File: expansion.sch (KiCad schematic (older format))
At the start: 4 parts, among them J10 Conn_02x05_Odd_Even, J7 DF40HC(3.5)-60DS, J9 DF40HC(3.5)-60DS, U1 IMX8MM

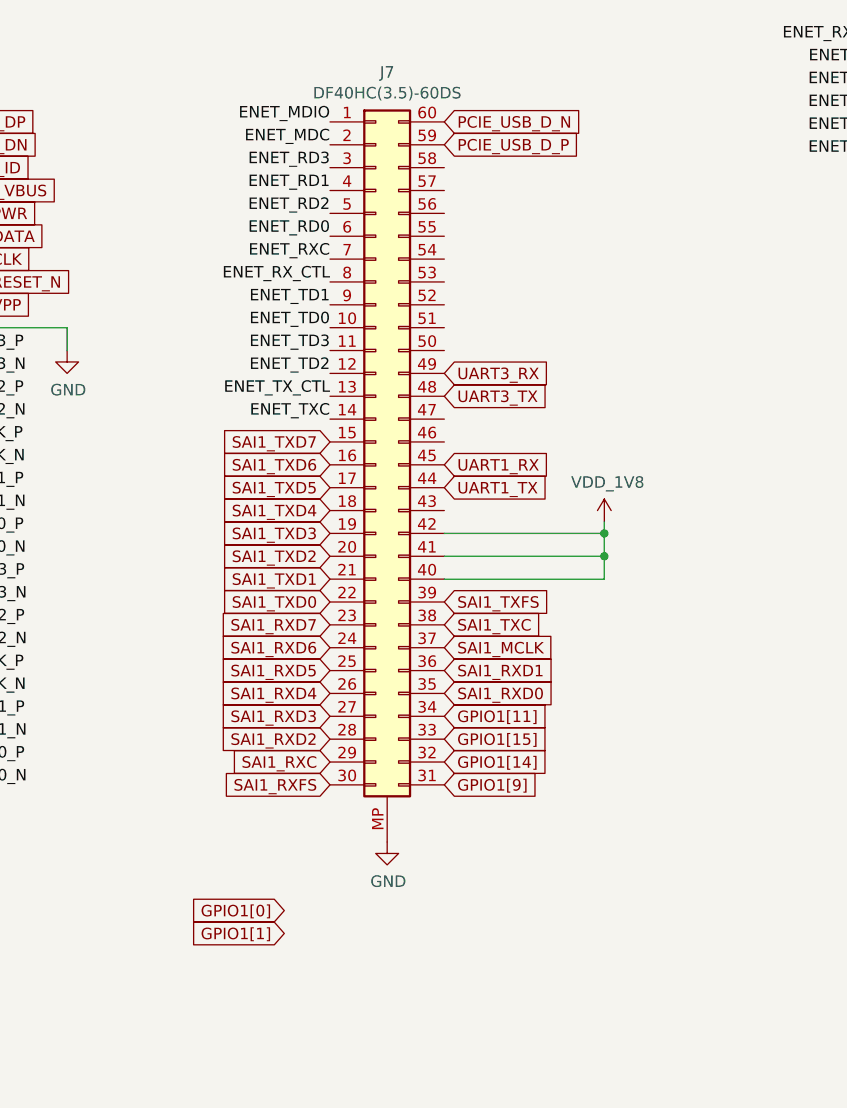
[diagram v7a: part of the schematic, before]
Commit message: prior to rerouting sai lanes
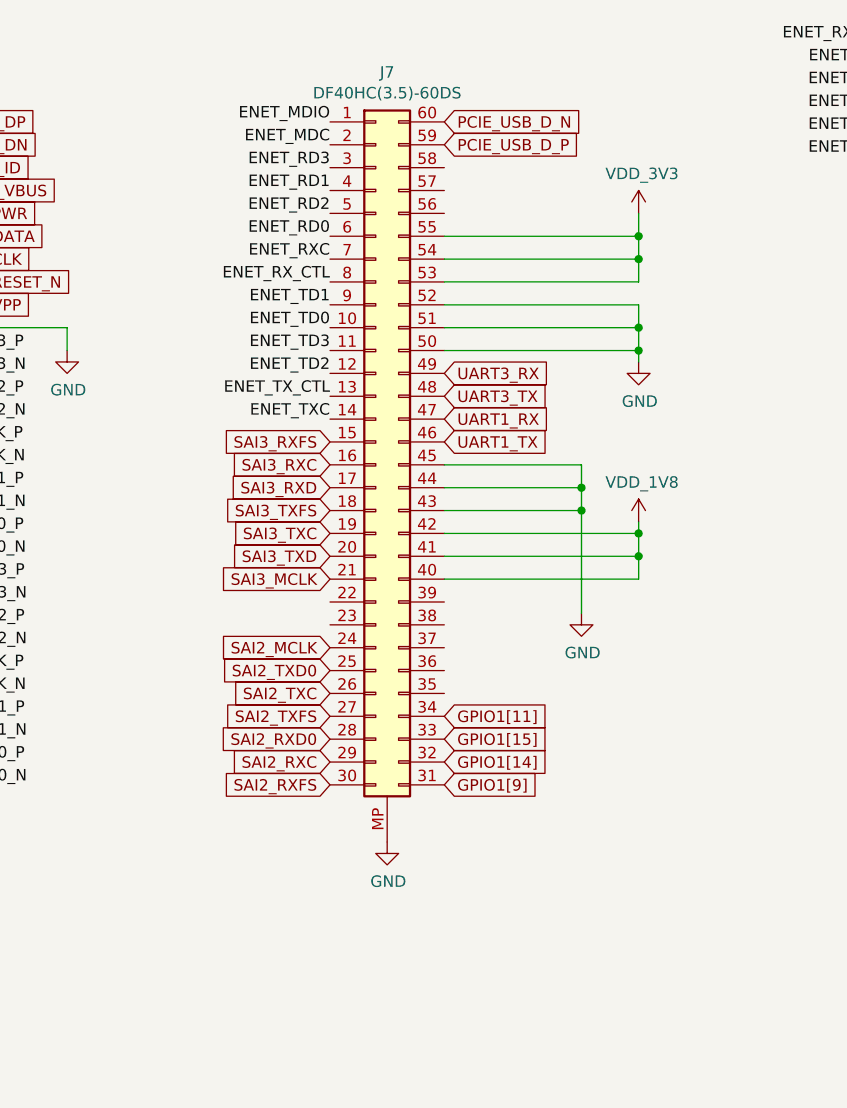
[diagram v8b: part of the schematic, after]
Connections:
- net GND: now also J7.43 (Pin_43), J7.44 (Pin_44), J7.45 (Pin_45), J7.50 (Pin_50), J7.51 (Pin_51), J7.52 (Pin_52)
- net UART1_RX: now also J7.47 (Pin_47); no longer J7.45 (Pin_45)
- net UART1_TX: now also J7.46 (Pin_46); no longer J7.44 (Pin_44)
- net VDD_3V3: now reaches J7.53 (Pin_53)
- net VDD_3V3: now also J7.54 (Pin_54), J7.55 (Pin_55)
- net SAI1_MCLK: no longer names the net of J7.37 (Pin_37)
- net SAI1_RXC renamed SAI2_RXC
- net SAI1_RXD0: no longer names the net of J7.35 (Pin_35)
- net SAI1_RXD1: no longer names the net of J7.36 (Pin_36)
- net SAI1_RXD2 renamed SAI2_RXD0
- net SAI1_RXD3 renamed SAI2_TXFS
- net SAI1_RXD4 renamed SAI2_TXC
- net SAI1_RXD5 renamed SAI2_TXD0
- net SAI1_RXD6 renamed SAI2_MCLK
- net SAI1_RXD7: no longer names the net of J7.23 (Pin_23)
- net SAI1_RXFS renamed SAI2_RXFS
- net SAI1_TXC: no longer names the net of J7.38 (Pin_38)
- net SAI1_TXD0: no longer names the net of J7.22 (Pin_22)
- net SAI1_TXD1 renamed SAI3_MCLK
- net SAI1_TXD2 renamed SAI3_TXD
- net SAI1_TXD3 renamed SAI3_TXC
- net SAI1_TXD4 renamed SAI3_TXFS
- net SAI1_TXD5 renamed SAI3_RXD
- net SAI1_TXD6 renamed SAI3_RXC
- net SAI1_TXD7 renamed SAI3_RXFS
- net SAI1_TXFS: no longer names the net of J7.39 (Pin_39)
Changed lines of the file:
@@
 Text Label 2750 2700 0    50   ~ 0
 GPIO3[17]
-Text GLabel 6550 6000 0    50   Input ~ 0
-GPIO1[0]
-Text GLabel 6550 6100 0    50   Input ~ 0
-GPIO1[1]
 $Comp
 L mxenc:MIMX8MM6DVTLZAA U1
@@
 Text Label 6750 2750 2    50   ~ 0
 ENET_RD3
-Text GLabel 6750 3950 0    50   Input ~ 0
-SAI1_TXD7
-Text GLabel 6750 4050 0    50   Input ~ 0
-SAI1_TXD6
-Text GLabel 6750 4150 0    50   Input ~ 0
-SAI1_TXD5
-Text GLabel 6750 4250 0    50   Input ~ 0
-SAI1_TXD4
-Text GLabel 6750 4350 0    50   Input ~ 0
-SAI1_TXD3
-Text GLabel 6750 4450 0    50   Input ~ 0
-SAI1_TXD2
-Text GLabel 6750 4550 0    50   Input ~ 0
-SAI1_TXD1
-Text GLabel 6750 4650 0    50   Input ~ 0
-SAI1_TXD0
-Text GLabel 6750 4750 0    50   Input ~ 0
-SAI1_RXD7
-Text GLabel 6750 4850 0    50   Input ~ 0
-SAI1_RXD6
-Text GLabel 6750 4950 0    50   Input ~ 0
-SAI1_RXD5
-Text GLabel 6750 5050 0    50   Input ~ 0
-SAI1_RXD4
-Text GLabel 6750 5150 0    50   Input ~ 0
-SAI1_RXD3
-Text GLabel 6750 5250 0    50   Input ~ 0
-SAI1_RXD2
-Text GLabel 6750 5350 0    50   Input ~ 0
-SAI1_RXC
-Text GLabel 6750 5450 0    50   Input ~ 0
-SAI1_RXFS
-Text GLabel 7250 4950 2    50   Input ~ 0
-SAI1_RXD1
-Text GLabel 7250 5050 2    50   Input ~ 0
-SAI1_RXD0
-Text GLabel 7250 4750 2    50   Input ~ 0
-SAI1_TXC
-Text GLabel 7250 4650 2    50   Input ~ 0
-SAI1_TXFS
-Text GLabel 7250 4850 2    50   Input ~ 0
-SAI1_MCLK
 Text Label 2750 2800 0    50   ~ 0
 GPIO3[18]
@@
 L mxenc:VDD_1V8 #PWR0223
 U 1 1 5F46F757
-P 7950 4300
-F 0 "#PWR0223" H 7950 4150 50  0001 C CNN
-F 1 "VDD_1V8" H 7965 4473 50  0000 C CNN
-F 2 "" H 7950 4300 50  0001 C CNN
-F 3 "" H 7950 4300 50  0001 C CNN
-	1    7950 4300
-	1    0    0    -1
-$EndComp
-Wire Wire Line
-	7950 4300 7950 4350
-Wire Wire Line
-	7950 4550 7250 4550
-Wire Wire Line
-	7250 4450 7950 4450
-Connection ~ 7950 4450
-Wire Wire Line
-	7950 4450 7950 4550
-Wire Wire Line
-	7950 4350 7250 4350
-Connection ~ 7950 4350
-Wire Wire Line
-	7950 4350 7950 4450
+P 8100 4300
+F 0 "#PWR0223" H 8100 4150 50  0001 C CNN
+F 1 "VDD_1V8" H 8115 4473 50  0000 C CNN
+F 2 "" H 8100 4300 50  0001 C CNN
+F 3 "" H 8100 4300 50  0001 C CNN
+	1    8100 4300
+	1    0    0    -1
+$EndComp
+Wire Wire Line
+	8100 4300 8100 4350
+Wire Wire Line
+	8100 4550 7250 4550
+Wire Wire Line
+	7250 4450 8100 4450
+Connection ~ 8100 4450
+Wire Wire Line
+	8100 4450 8100 4550
+Wire Wire Line
+	8100 4350 7250 4350
+Connection ~ 8100 4350
+Wire Wire Line
+	8100 4350 8100 4450
 Text GLabel 7250 2550 2    50   Input ~ 0
 PCIE_USB_D_N
@@
 Text GLabel 7250 3650 2    50   Input ~ 0
 UART3_RX
-Text GLabel 7250 4050 2    50   Input ~ 0
+Text GLabel 7250 3850 2    50   Input ~ 0
 UART1_RX
-Text GLabel 7250 4150 2    50   Input ~ 0
+Text GLabel 7250 3950 2    50   Input ~ 0
 UART1_TX
 $Comp
@@
 Text GLabel 7250 5250 2    50   Input ~ 0
 GPIO1[15]
+$Comp
+L power:GND #PWR0222
+U 1 1 5EFF4815
+P 7850 4700
+F 0 "#PWR0222" H 7850 4450 50  0001 C CNN
+F 1 "GND" H 7855 4527 50  0000 C CNN
+F 2 "" H 7850 4700 50  0001 C CNN
+F 3 "" H 7850 4700 50  0001 C CNN
+	1    7850 4700
+	1    0    0    -1
+$EndComp
+Wire Wire Line
+	7250 4250 7850 4250
+Wire Wire Line
+	7850 4250 7850 4700
+Wire Wire Line
+	7250 4050 7850 4050
+Wire Wire Line
+	7850 4050 7850 4150
+Connection ~ 7850 4250
+Wire Wire Line
+	7250 4150 7850 4150
+Connection ~ 7850 4150
+Wire Wire Line
+	7850 4150 7850 4250
+$Comp
+L mxenc:VDD_3V3 #PWR0245
+U 1 1 5F185D48
+P 8100 2950
+F 0 "#PWR0245" H 8100 2800 50  0001 C CNN
+F 1 "VDD_3V3" H 8115 3123 50  0000 C CNN
+F 2 "" H 8100 2950 50  0001 C CNN
+F 3 "" H 8100 2950 50  0001 C CNN
+	1    8100 2950
+	1    0    0    -1
+$EndComp
+Wire Wire Line
+	8100 2950 8100 3050
+Wire Wire Line
+	8100 3050 7250 3050
+Wire Wire Line
+	8100 3050 8100 3150
+Wire Wire Line
+	8100 3150 7250 3150
+Connection ~ 8100 3050
+Wire Wire Line
+	7250 3250 8100 3250
+Wire Wire Line
+	8100 3250 8100 3150
+Connection ~ 8100 3150
+$Comp
+L power:GND #PWR0253
+U 1 1 5F18CEE2
+P 8100 3600
+F 0 "#PWR0253" H 8100 3350 50  0001 C CNN
+F 1 "GND" H 8105 3427 50  0000 C CNN
+F 2 "" H 8100 3600 50  0001 C CNN
+F 3 "" H 8100 3600 50  0001 C CNN
+	1    8100 3600
+	1    0    0    -1
+$EndComp
+Wire Wire Line
+	8100 3600 8100 3550
+Wire Wire Line
+	8100 3350 7250 3350
+Wire Wire Line
+	7250 3450 8100 3450
+Connection ~ 8100 3450
+Wire Wire Line
+	8100 3450 8100 3350
+Connection ~ 8100 3550
+Wire Wire Line
+	8100 3550 8100 3450
+Wire Wire Line
+	7250 3550 8100 3550
+Text GLabel 6750 4550 0    50   Input ~ 0
+SAI3_MCLK
+Text GLabel 6750 4450 0    50   Input ~ 0
+SAI3_TXD
+Text GLabel 6750 4350 0    50   Input ~ 0
+SAI3_TXC
+Text GLabel 6750 4250 0    50   Input ~ 0
+SAI3_TXFS
+Text GLabel 6750 4150 0    50   Input ~ 0
+SAI3_RXD
+Text GLabel 6750 4050 0    50   Input ~ 0
+SAI3_RXC
+Text GLabel 6750 3950 0    50   Input ~ 0
+SAI3_RXFS
+Text GLabel 6750 4850 0    50   Input ~ 0
+SAI2_MCLK
+Text GLabel 6750 4950 0    50   Input ~ 0
+SAI2_TXD0
+Text GLabel 6750 5050 0    50   Input ~ 0
+SAI2_TXC
+Text GLabel 6750 5150 0    50   Input ~ 0
+SAI2_TXFS
+Text GLabel 6750 5250 0    50   Input ~ 0
+SAI2_RXD0
+Text GLabel 6750 5350 0    50   Input ~ 0
+SAI2_RXC
+Text GLabel 6750 5450 0    50   Input ~ 0
+SAI2_RXFS
 $EndSCHEMATC
